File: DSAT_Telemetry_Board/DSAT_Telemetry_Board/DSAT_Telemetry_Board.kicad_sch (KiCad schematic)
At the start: 0 parts

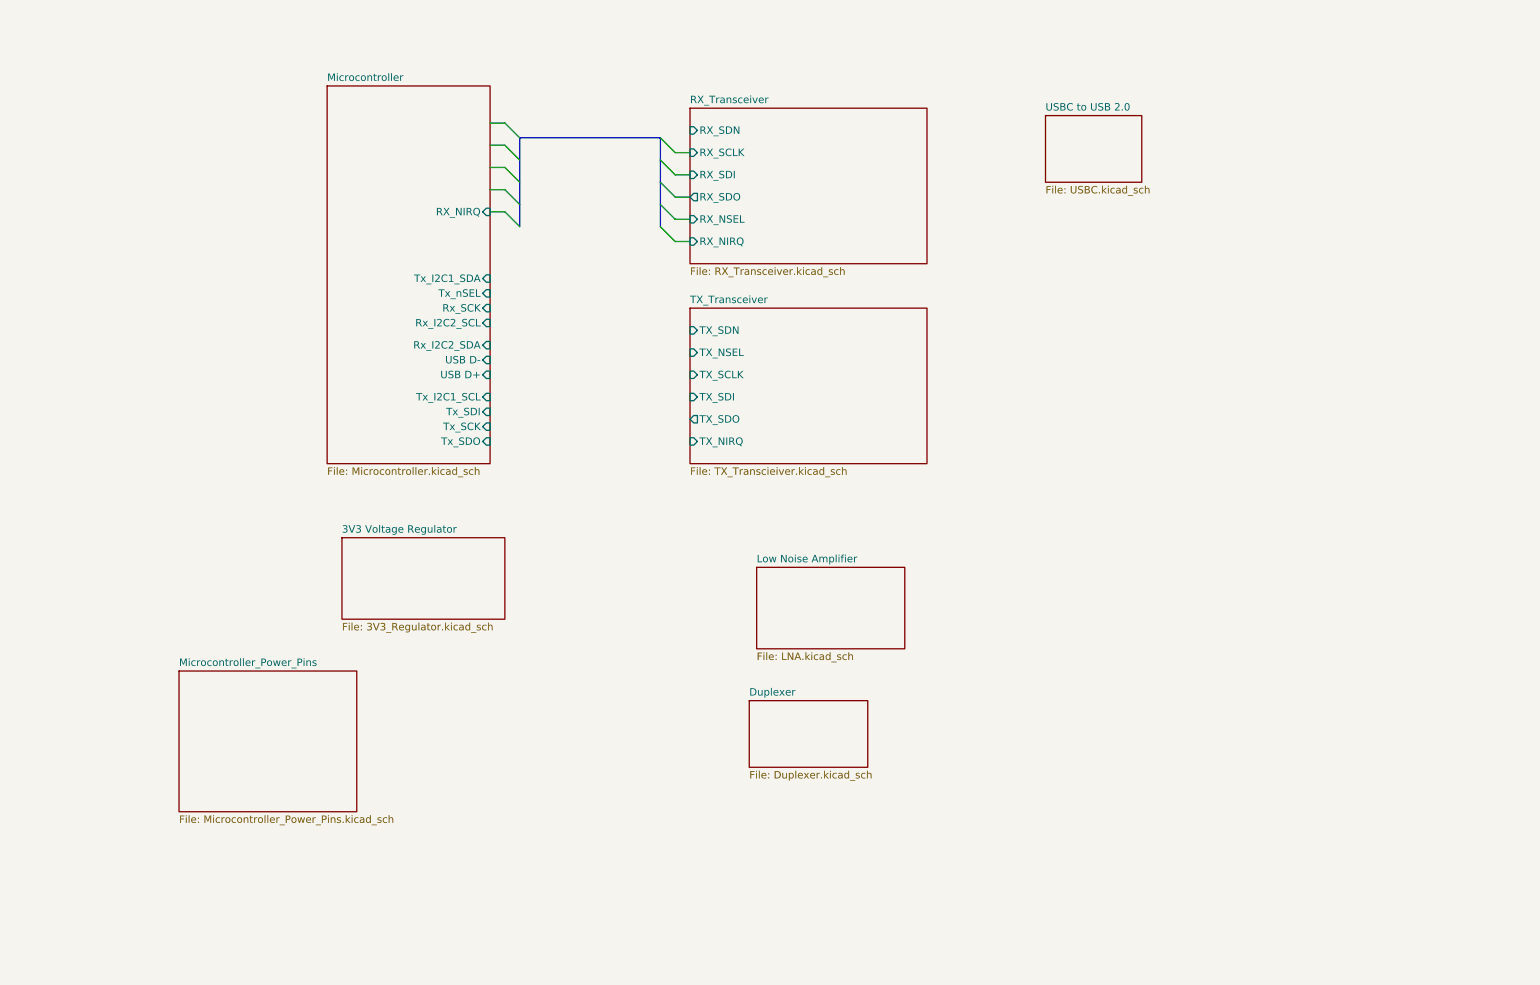
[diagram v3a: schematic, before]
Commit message: Updated Microcontroller Pinout Names
Updated Names
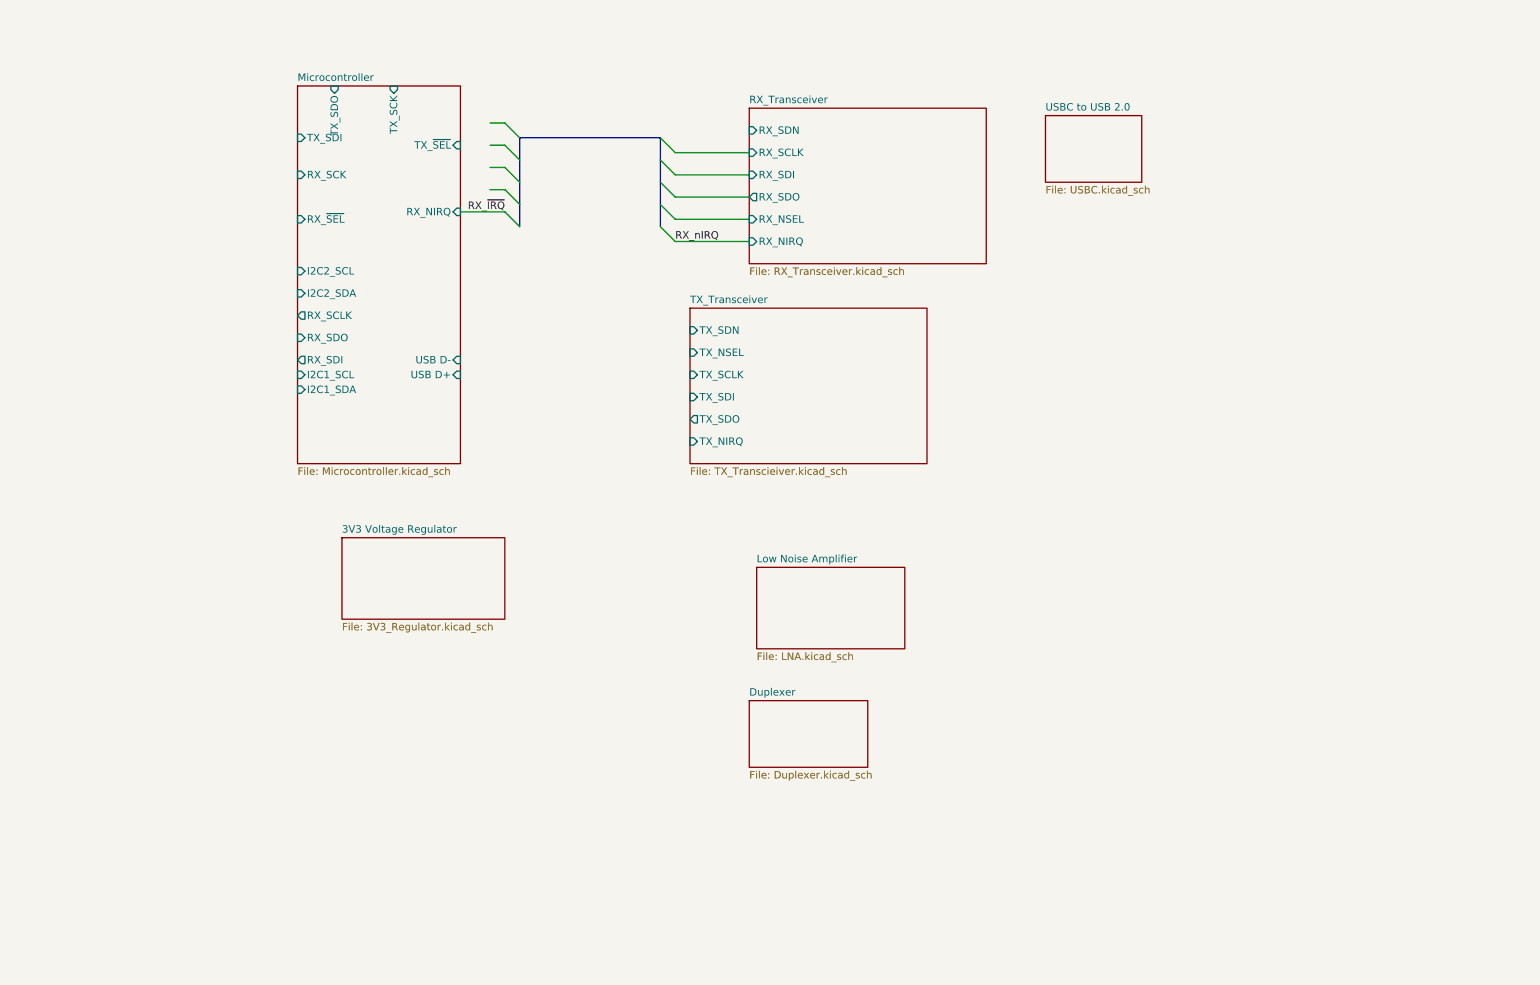
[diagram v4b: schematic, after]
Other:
- removed sheet Microcontroller_Power_Pins
- sheet Microcontroller ports: added I2C1_SCL, I2C1_SDA, I2C2_SCL, I2C2_SDA, RX_SCK, RX_SCLK, RX_SDI, RX_SDO, RX_~{SEL}, TX_SCK, TX_SDI, TX_SDO, TX_~{SEL}; removed Rx_I2C2_SCL, Rx_I2C2_SDA, Rx_SCK, Tx_I2C1_SCL, Tx_I2C1_SDA, Tx_SCK, Tx_SDI, Tx_SDO, Tx_nSEL
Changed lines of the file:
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@@
     (stroke (width 0) (type default) (color 0 0 0 0))
   )
-  (wire (pts (xy 135.89 44.45) (xy 138.43 44.45))
+  (wire (pts (xy 135.89 44.45) (xy 148.59 44.45))
     (stroke (width 0) (type default) (color 0 0 0 0))
   )
@@
     (stroke (width 0) (type default) (color 0 0 0 0))
   )
-  (wire (pts (xy 135.89 48.26) (xy 138.43 48.26))
+  (wire (pts (xy 135.89 48.26) (xy 148.59 48.26))
     (stroke (width 0) (type default) (color 0 0 0 0))
   )
@@
     (stroke (width 0) (type default) (color 0 0 0 0))
   )
-  (wire (pts (xy 135.89 59.69) (xy 138.43 59.69))
-    (stroke (width 0) (type default) (color 0 0 0 0))
-  )
-  (wire (pts (xy 135.89 52.07) (xy 138.43 52.07))
+  (wire (pts (xy 135.89 59.69) (xy 148.59 59.69))
+    (stroke (width 0) (type default) (color 0 0 0 0))
+  )
+  (wire (pts (xy 135.89 52.07) (xy 148.59 52.07))
     (stroke (width 0) (type default) (color 0 0 0 0))
   )
@@
     (stroke (width 0) (type default) (color 0 0 0 0))
   )
-  (wire (pts (xy 135.89 55.88) (xy 138.43 55.88))
+  (wire (pts (xy 135.89 55.88) (xy 148.59 55.88))
     (stroke (width 0) (type default) (color 0 0 0 0))
   )
@@
     (stroke (width 0) (type default) (color 0 0 0 0))
   )
-  (wire (pts (xy 104.14 54.61) (xy 106.68 54.61))
+  (wire (pts (xy 99.06 54.61) (xy 106.68 54.61))
     (stroke (width 0) (type default) (color 0 0 0 0))
   )
@@
     (stroke (width 0) (type default) (color 0 0 0 0))
   )
+  (label "RX_~{IRQ}" (at 100.33 54.61 0)
+    (effects (font (size 1.27 1.27)) (justify left bottom))
+  )
+  (label "RX_nIRQ" (at 135.89 59.69 0)
+    (effects (font (size 1.27 1.27)) (justify left bottom))
+  )
   (sheet (at 148.59 138.43) (size 20.32 11.43) (fields_autoplaced)
     (stroke (width 0.1524) (type solid) (color 0 0 0 0))
@@
     )
   )
-  (sheet (at 138.43 36.83) (size 40.64 26.67) (fields_autoplaced)
-    (stroke (width 0.1524) (type solid) (color 0 0 0 0))
-    (fill (color 0 0 0 0.0000))
-    (property "Sheet name" "RX_Transceiver" (id 0) (at 138.43 36.1184 0)
-      (effects (font (size 1.27 1.27)) (justify left bottom))
-    )
-    (property "Sheet file" "RX_Transceiver.kicad_sch" (id 1) (at 138.43 64.0846 0)
-      (effects (font (size 1.27 1.27)) (justify left top))
-    )
-    (pin "RX_SDN" input (at 138.43 40.64 180)
-      (effects (font (size 1.27 1.27)) (justify left))
-    )
-    (pin "RX_SCLK" input (at 138.43 44.45 180)
-      (effects (font (size 1.27 1.27)) (justify left))
-    )
-    (pin "RX_SDI" input (at 138.43 48.26 180)
-      (effects (font (size 1.27 1.27)) (justify left))
-    )
-    (pin "RX_SDO" output (at 138.43 52.07 180)
-      (effects (font (size 1.27 1.27)) (justify left))
-    )
-    (pin "RX_NSEL" input (at 138.43 55.88 180)
-      (effects (font (size 1.27 1.27)) (justify left))
-    )
-    (pin "RX_NIRQ" input (at 138.43 59.69 180)
+  (sheet (at 148.59 36.83) (size 40.64 26.67) (fields_autoplaced)
+    (stroke (width 0.1524) (type solid) (color 0 0 0 0))
+    (fill (color 0 0 0 0.0000))
+    (property "Sheet name" "RX_Transceiver" (id 0) (at 148.59 36.1184 0)
+      (effects (font (size 1.27 1.27)) (justify left bottom))
+    )
+    (property "Sheet file" "RX_Transceiver.kicad_sch" (id 1) (at 148.59 64.0846 0)
+      (effects (font (size 1.27 1.27)) (justify left top))
+    )
+    (pin "RX_SDN" input (at 148.59 40.64 180)
+      (effects (font (size 1.27 1.27)) (justify left))
+    )
+    (pin "RX_SCLK" input (at 148.59 44.45 180)
+      (effects (font (size 1.27 1.27)) (justify left))
+    )
+    (pin "RX_SDI" input (at 148.59 48.26 180)
+      (effects (font (size 1.27 1.27)) (justify left))
+    )
+    (pin "RX_SDO" output (at 148.59 52.07 180)
+      (effects (font (size 1.27 1.27)) (justify left))
+    )
+    (pin "RX_NSEL" input (at 148.59 55.88 180)
+      (effects (font (size 1.27 1.27)) (justify left))
+    )
+    (pin "RX_NIRQ" input (at 148.59 59.69 180)
       (effects (font (size 1.27 1.27)) (justify left))
     )
@@
     )
   )
-  (sheet (at 50.8 133.35) (size 30.48 24.13) (fields_autoplaced)
-    (stroke (width 0.1524) (type solid) (color 0 0 0 0))
-    (fill (color 0 0 0 0.0000))
-    (property "Sheet name" "Microcontroller_Power_Pins" (id 0) (at 50.8 132.6384 0)
-      (effects (font (size 1.27 1.27)) (justify left bottom))
-    )
-    (property "Sheet file" "Microcontroller_Power_Pins.kicad_sch" (id 1) (at 50.8 158.0646 0)
-      (effects (font (size 1.27 1.27)) (justify left top))
-    )
-  )
-  (sheet (at 76.2 33.02) (size 27.94 64.77) (fields_autoplaced)
-    (stroke (width 0.1524) (type solid) (color 0 0 0 0))
-    (fill (color 0 0 0 0.0000))
-    (property "Sheet name" "Microcontroller" (id 0) (at 76.2 32.3084 0)
-      (effects (font (size 1.27 1.27)) (justify left bottom))
-    )
-    (property "Sheet file" "Microcontroller.kicad_sch" (id 1) (at 76.2 98.3746 0)
-      (effects (font (size 1.27 1.27)) (justify left top))
-    )
-    (pin "RX_NIRQ" input (at 104.14 54.61 0)
-      (effects (font (size 1.27 1.27)) (justify right))
-    )
-    (pin "Rx_SCK" input (at 104.14 71.12 0)
-      (effects (font (size 1.27 1.27)) (justify right))
-    )
-    (pin "Rx_I2C2_SCL" input (at 104.14 73.66 0)
-      (effects (font (size 1.27 1.27)) (justify right))
-    )
-    (pin "Rx_I2C2_SDA" input (at 104.14 77.47 0)
-      (effects (font (size 1.27 1.27)) (justify right))
-    )
-    (pin "USB D-" input (at 104.14 80.01 0)
-      (effects (font (size 1.27 1.27)) (justify right))
-    )
-    (pin "USB D+" input (at 104.14 82.55 0)
-      (effects (font (size 1.27 1.27)) (justify right))
-    )
-    (pin "Tx_I2C1_SCL" input (at 104.14 86.36 0)
-      (effects (font (size 1.27 1.27)) (justify right))
-    )
-    (pin "Tx_SDI" input (at 104.14 88.9 0)
-      (effects (font (size 1.27 1.27)) (justify right))
-    )
-    (pin "Tx_SCK" input (at 104.14 91.44 0)
-      (effects (font (size 1.27 1.27)) (justify right))
-    )
-    (pin "Tx_SDO" input (at 104.14 93.98 0)
-      (effects (font (size 1.27 1.27)) (justify right))
-    )
-    (pin "Tx_nSEL" input (at 104.14 68.58 0)
-      (effects (font (size 1.27 1.27)) (justify right))
-    )
-    (pin "Tx_I2C1_SDA" input (at 104.14 66.04 0)
+  (sheet (at 71.12 33.02) (size 27.94 64.77) (fields_autoplaced)
+    (stroke (width 0.1524) (type solid) (color 0 0 0 0))
+    (fill (color 0 0 0 0.0000))
+    (property "Sheet name" "Microcontroller" (id 0) (at 71.12 32.3084 0)
+      (effects (font (size 1.27 1.27)) (justify left bottom))
+    )
+    (property "Sheet file" "Microcontroller.kicad_sch" (id 1) (at 71.12 98.3746 0)
+      (effects (font (size 1.27 1.27)) (justify left top))
+    )
+    (pin "RX_NIRQ" input (at 99.06 54.61 0)
+      (effects (font (size 1.27 1.27)) (justify right))
+    )
+    (pin "USB D-" input (at 99.06 80.01 0)
+      (effects (font (size 1.27 1.27)) (justify right))
+    )
+    (pin "USB D+" input (at 99.06 82.55 0)
+      (effects (font (size 1.27 1.27)) (justify right))
+    )
+    (pin "I2C2_SCL" input (at 71.12 64.77 180)
+      (effects (font (size 1.27 1.27)) (justify left))
+    )
+    (pin "I2C2_SDA" input (at 71.12 68.58 180)
+      (effects (font (size 1.27 1.27)) (justify left))
+    )
+    (pin "RX_SCLK" output (at 71.12 72.39 180)
+      (effects (font (size 1.27 1.27)) (justify left))
+    )
+    (pin "RX_SDO" input (at 71.12 76.2 180)
+      (effects (font (size 1.27 1.27)) (justify left))
+    )
+    (pin "RX_SDI" output (at 71.12 80.01 180)
+      (effects (font (size 1.27 1.27)) (justify left))
+    )
+    (pin "I2C1_SCL" input (at 71.12 82.55 180)
+      (effects (font (size 1.27 1.27)) (justify left))
+    )
+    (pin "I2C1_SDA" input (at 71.12 85.09 180)
+      (effects (font (size 1.27 1.27)) (justify left))
+    )
+    (pin "RX_~{SEL}" input (at 71.12 55.88 180)
+      (effects (font (size 1.27 1.27)) (justify left))
+    )
+    (pin "RX_SCK" input (at 71.12 48.26 180)
+      (effects (font (size 1.27 1.27)) (justify left))
+    )
+    (pin "TX_SDI" input (at 71.12 41.91 180)
+      (effects (font (size 1.27 1.27)) (justify left))
+    )
+    (pin "TX_SDO" input (at 77.47 33.02 90)
+      (effects (font (size 1.27 1.27)) (justify right))
+    )
+    (pin "TX_SCK" input (at 87.63 33.02 90)
+      (effects (font (size 1.27 1.27)) (justify right))
+    )
+    (pin "TX_~{SEL}" input (at 99.06 43.18 0)
       (effects (font (size 1.27 1.27)) (justify right))
     )
@@
   (sheet_instances
     (path "/" (page "1"))
-    (path "/eded1b35-4e0f-4f00-ac10-8e3fc06300de" (page "2"))
     (path "/bd133518-b1d6-4b0c-831d-7da8fbce82c8" (page "3"))
     (path "/b35dd259-52b0-4d58-958d-7e3f75bcc749" (page "4"))

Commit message: Seperate Branch
Updated Pin names, Added LNA, Fixed Pins on USB connection
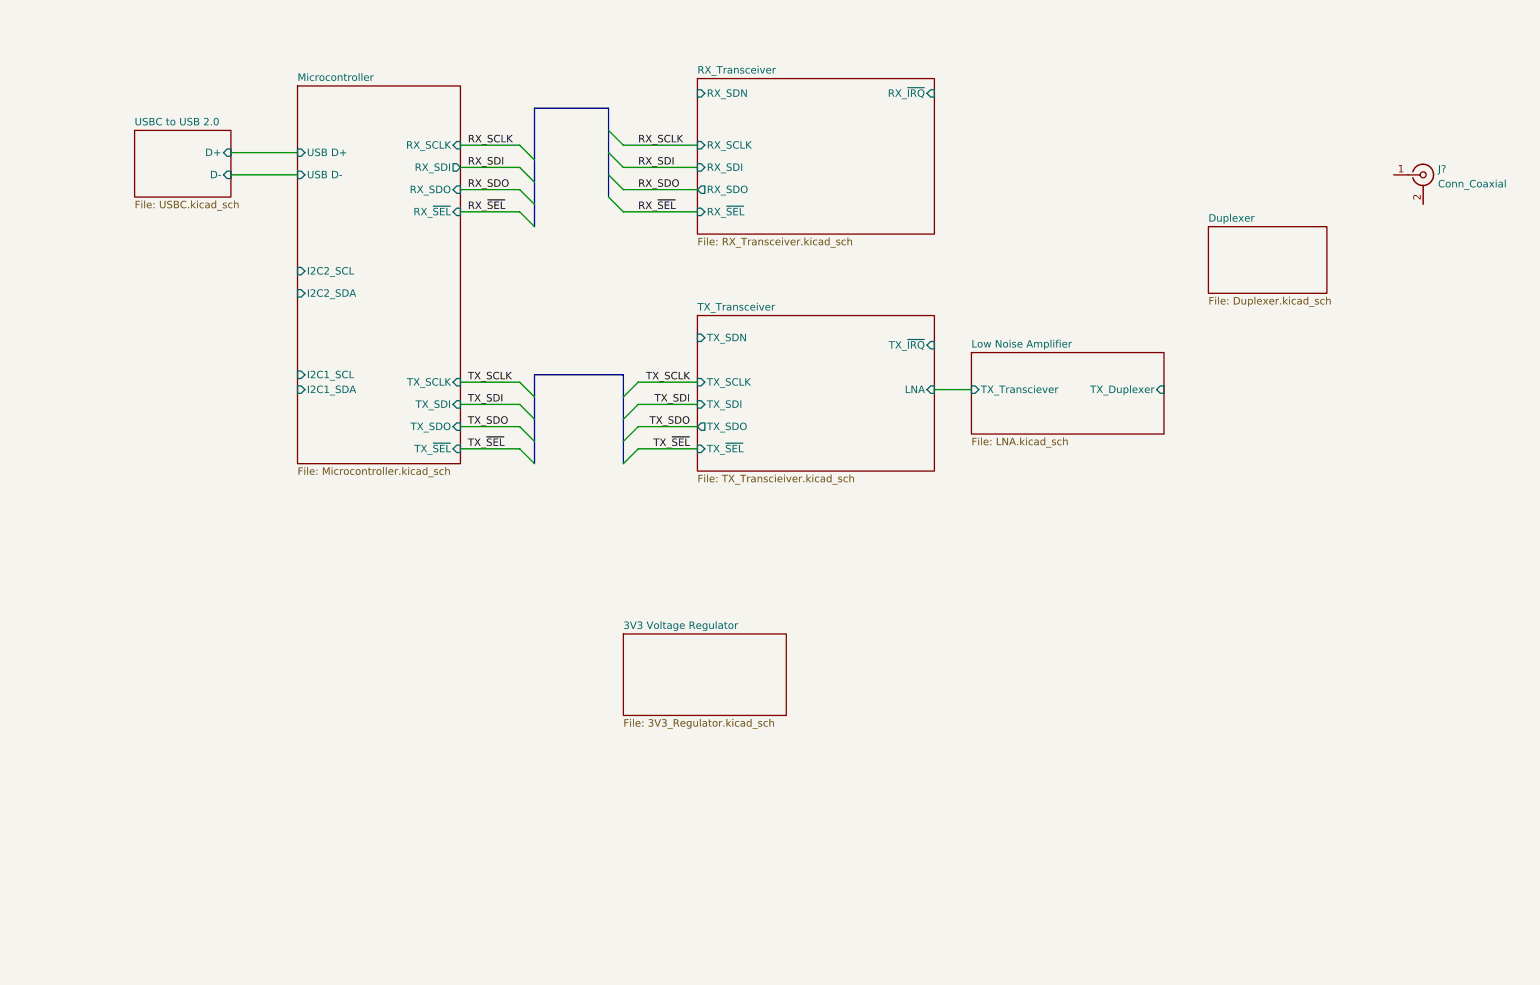
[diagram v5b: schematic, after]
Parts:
- added J?: Conn_Coaxial, symbol Connector:Conn_Coaxial
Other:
- sheet Low Noise Amplifier ports: added TX_Duplexer, TX_Transciever; removed none
- sheet Microcontroller ports: added TX_SCLK; removed RX_NIRQ, RX_SCK, TX_SCK
- sheet RX_Transceiver ports: added RX_~{IRQ}, RX_~{SEL}; removed RX_NIRQ, RX_NSEL
- sheet TX_Transceiver ports: added LNA, TX_~{IRQ}, TX_~{SEL}; removed TX_NIRQ, TX_NSEL
- sheet USBC to USB 2.0 ports: added D+, D-; removed none
